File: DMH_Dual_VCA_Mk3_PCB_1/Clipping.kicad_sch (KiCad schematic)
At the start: 26 parts, among them SW1 SW_DPDT_OnOffOn_x2, U8 TL074

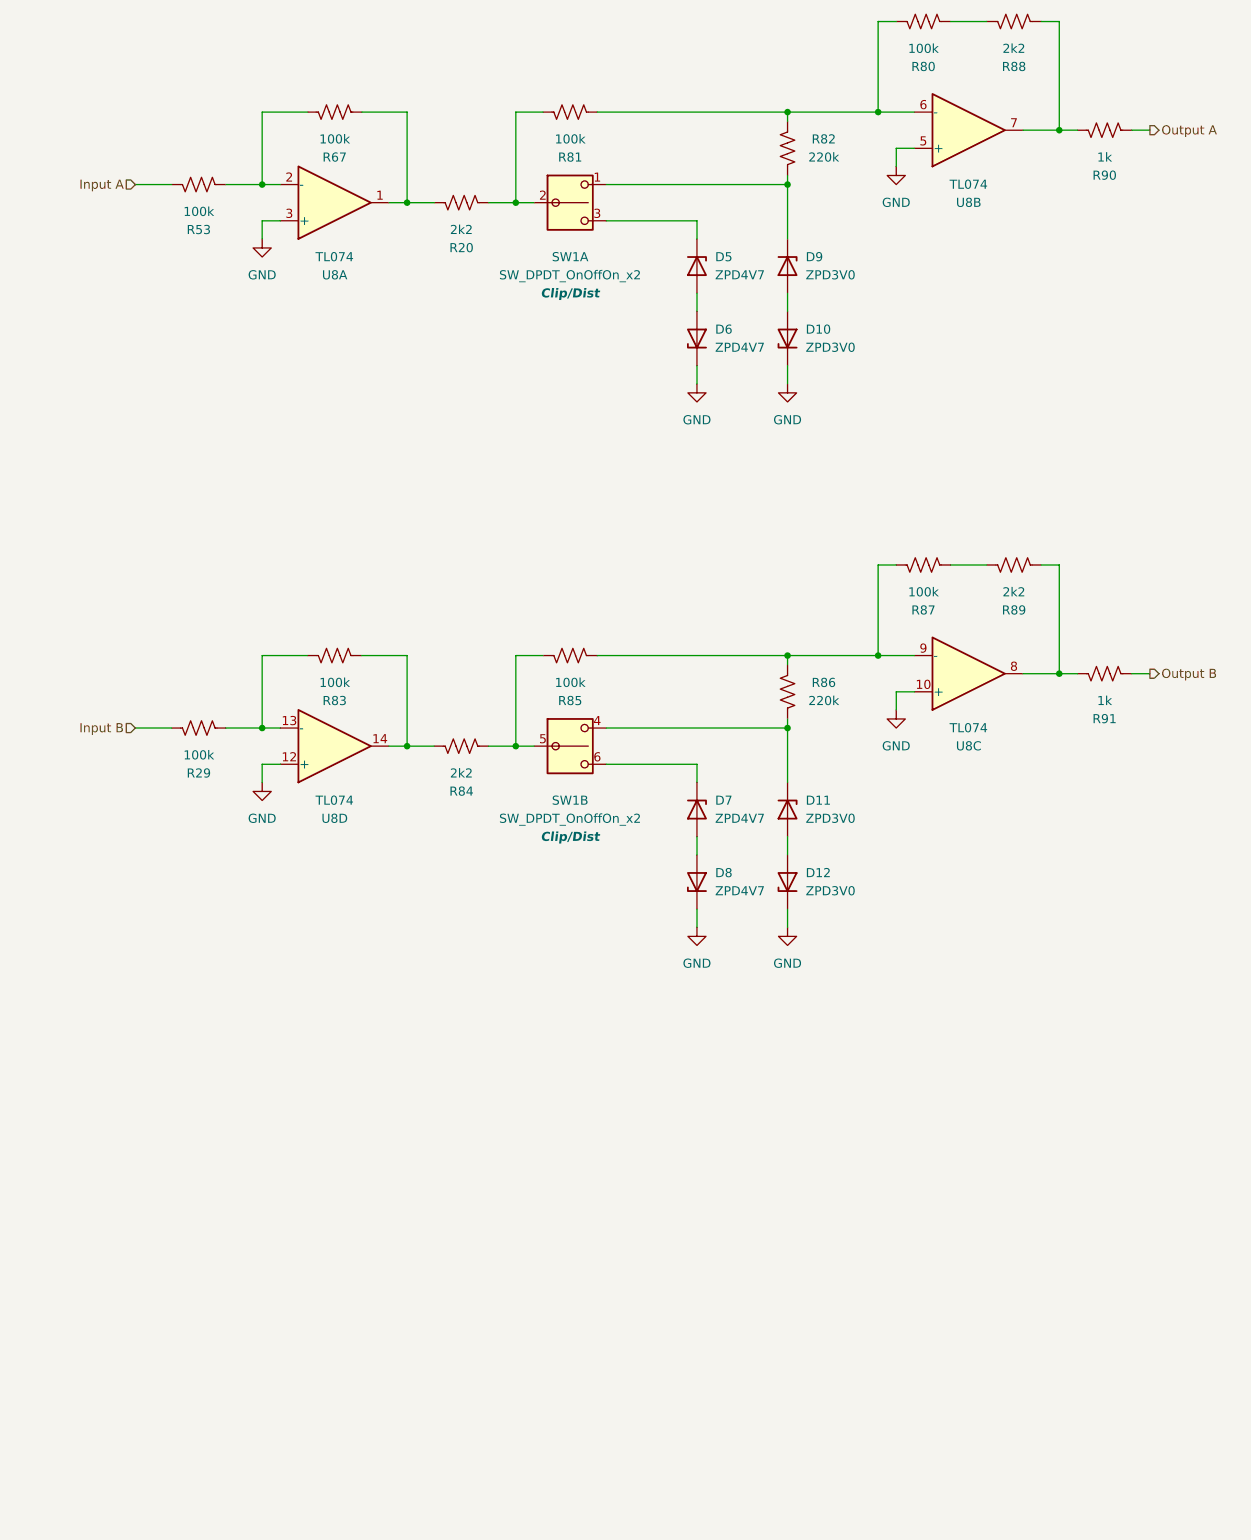
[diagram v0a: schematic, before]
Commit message: Added clipping LED to schematic
Still need to add to Panel
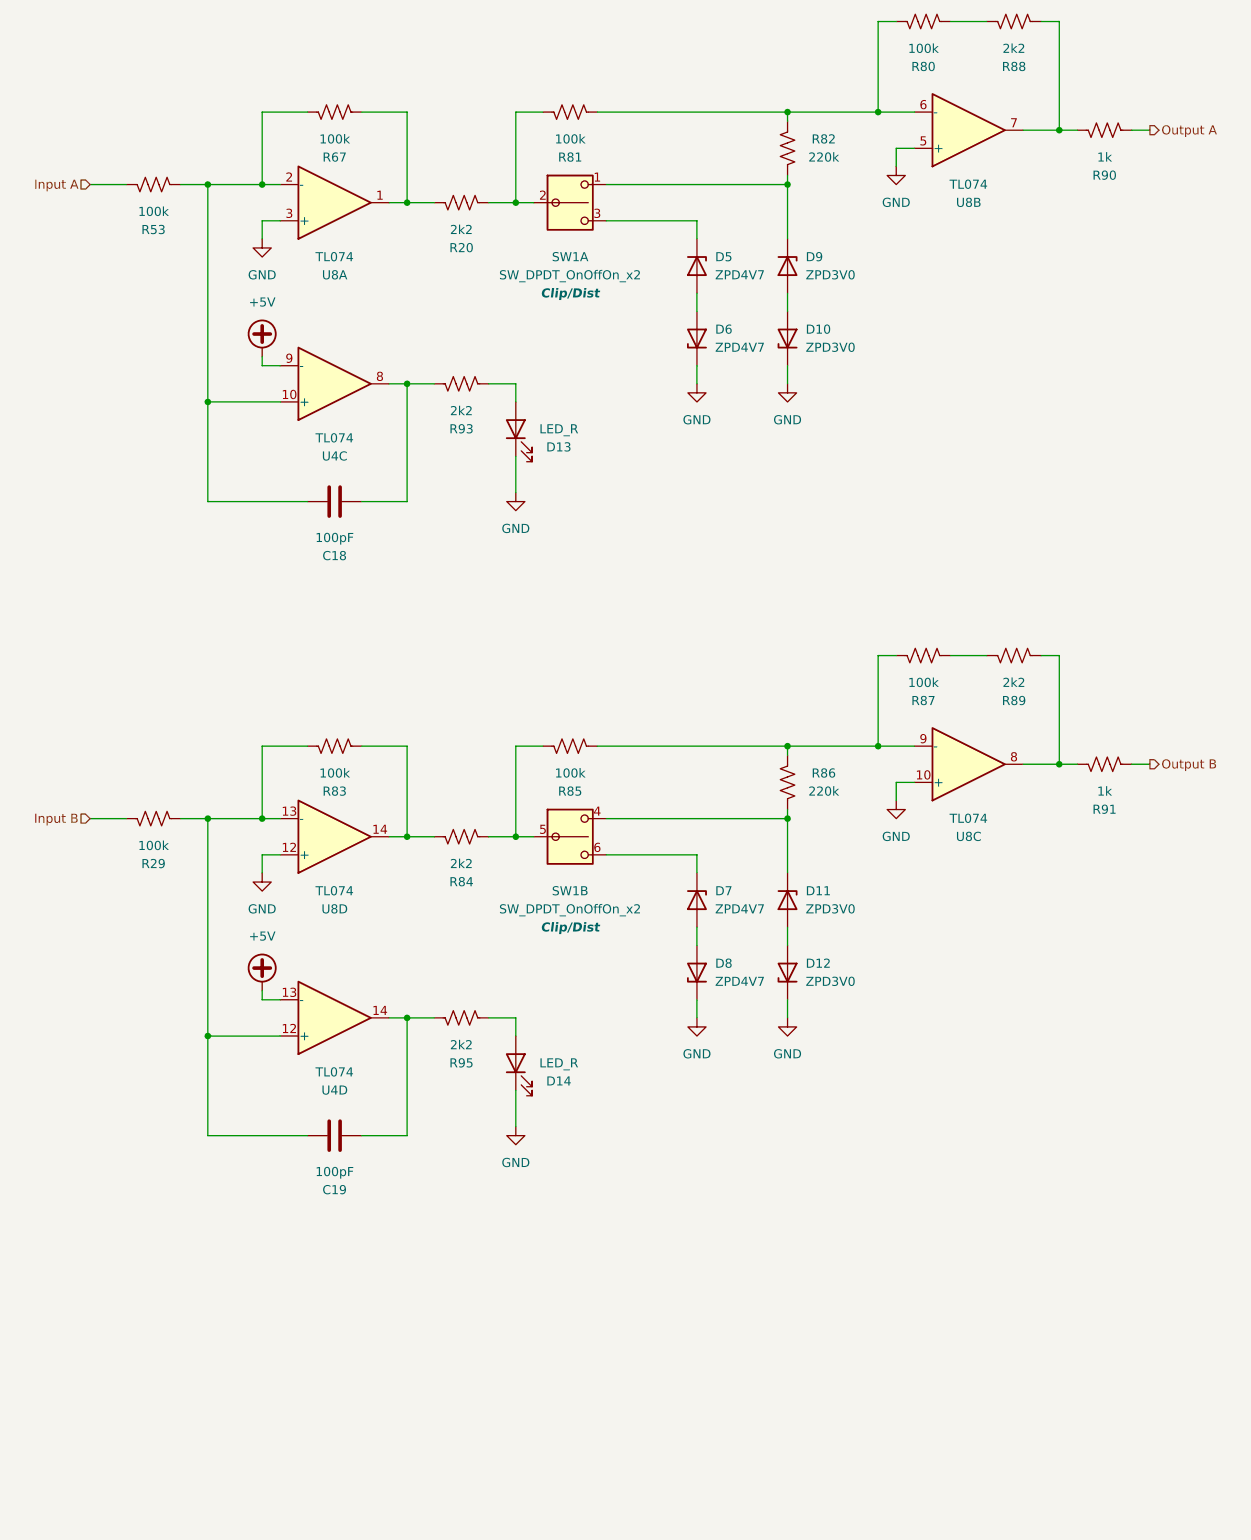
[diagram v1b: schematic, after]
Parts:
- added C18, C19: 100pF, Capacitor_THT:C_Disc_D3.0mm_W2.0mm_P2.50mm, symbol Device:C
- added D13, D14: LED_R, LED_THT:LED_D3.0mm, symbol Device:LED
- added R93, R95: 2k2, Resistor_THT:R_Axial_DIN0207_L6.3mm_D2.5mm_P7.62mm_Horizontal, symbol Device:R_US
- added U4: TL074, Package_DIP:DIP-14_W7.62mm_Socket, symbol Amplifier_Operational:TL074
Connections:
- net GND: now also D13.1 (K), D14.1 (K)
- net at R53.2, R67.2, U8.2 (-): now also C18.1, U4.10 (+)
- net at R29.2, R83.2, U8.13 (-): now also C19.1, U4.12 (+)
- new net: C19.2, R95.1, U4.14
- new net: D13.2 (A), R93.2
- new net: C18.2, R93.1, U4.8
- new net: D14.2 (A), R95.2
- new net +5V: U4.13 (-), U4.9 (-)
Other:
- moved on the sheet: D11, D12, D7, D8, R29, R53, R83, R84, R85, R86, R87, R89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

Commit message: Improved clipping indication
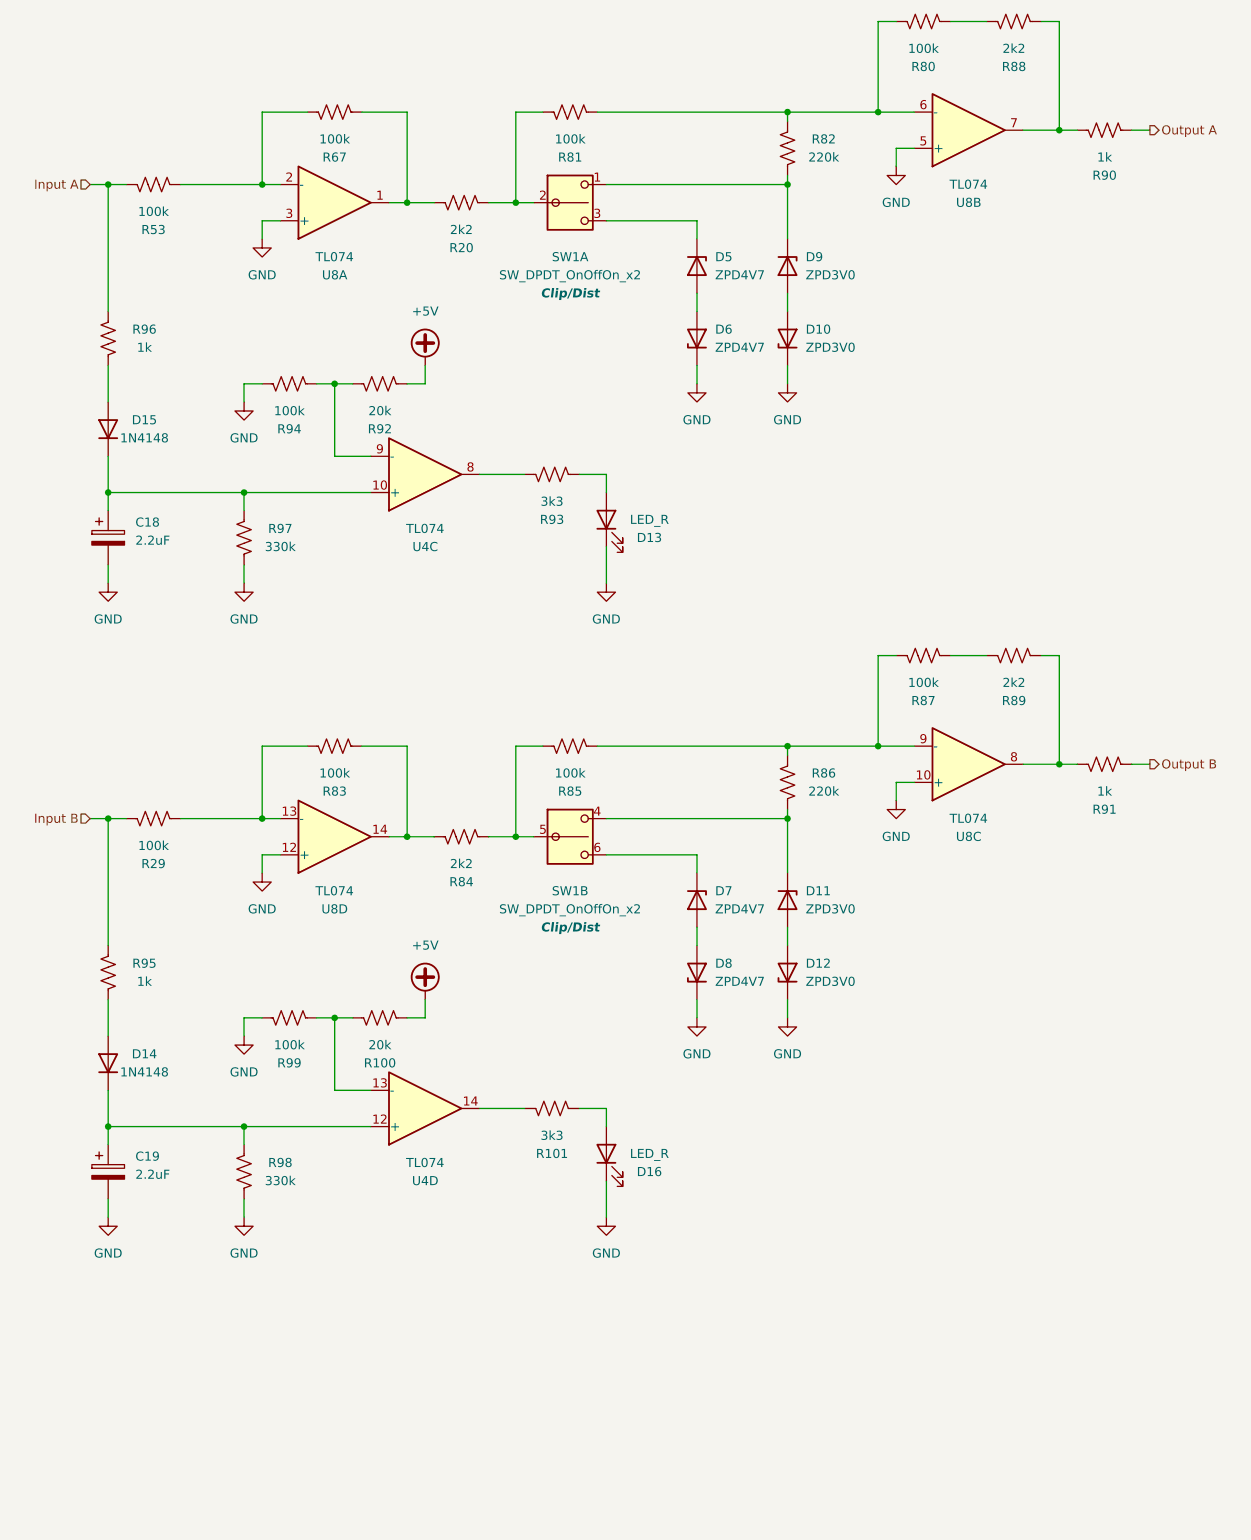
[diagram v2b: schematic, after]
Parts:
- removed C18, C19: 100pF, Capacitor_THT:C_Disc_D3.0mm_W2.0mm_P2.50mm, symbol Device:C
- removed D14: LED_R, LED_THT:LED_D3.0mm, symbol Device:LED
- added C18, C19: 2.2uF, Capacitor_THT:CP_Radial_D4.0mm_P1.50mm, symbol Device:C_Polarized
- added D14, D15: 1N4148, Diode_THT:D_DO-35_SOD27_P7.62mm_Horizontal, symbol Diode:1N4148
- added D16: LED_R, LED_THT:LED_D3.0mm, symbol Device:LED
- added R100, R92: 20k, Resistor_THT:R_Axial_DIN0207_L6.3mm_D2.5mm_P7.62mm_Horizontal, symbol Device:R_US
- added R101: 3k3, Resistor_THT:R_Axial_DIN0207_L6.3mm_D2.5mm_P7.62mm_Horizontal, symbol Device:R_US
- added R94, R99: 100k, Resistor_THT:R_Axial_DIN0207_L6.3mm_D2.5mm_P7.62mm_Horizontal, symbol Device:R_US
- added R96: 1k, Resistor_THT:R_Axial_DIN0207_L6.3mm_D2.5mm_P7.62mm_Horizontal, symbol Device:R_US
- added R97, R98: 330k, Resistor_THT:R_Axial_DIN0207_L6.3mm_D2.5mm_P7.62mm_Horizontal, symbol Device:R_US
- R93: value 2k2 -> 3k3
- R95: value 2k2 -> 1k
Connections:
- net +5V: now also R100.2, R92.2; no longer U4.13 (-), U4.9 (-)
- net GND: now also C18.2, C19.2, D16.1 (K), R94.1, R97.1, R98.1, R99.1
- net Input A: now also R96.2
- net Input B: now also R95.2
- net at R29.2, R83.2, U8.13 (-): no longer U4.12 (+)
- net at R95.1: now also D14.2 (A); no longer U4.14
- net at R53.2, R67.2, U8.2 (-): no longer U4.10 (+)
- new net: D15.2 (A), R96.1
- new net: C18.1, D15.1 (K), R97.2, U4.10 (+)
- new net: R92.1, R94.2, U4.9 (-)
- new net: D16.2 (A), R101.2
- new net: C19.1, D14.1 (K), R98.2, U4.12 (+)
- new net: R100.1, R99.2, U4.13 (-)
- new net: R101.1, U4.14
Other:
- moved on the sheet: D13, R93
